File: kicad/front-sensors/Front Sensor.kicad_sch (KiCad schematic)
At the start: 10 parts, among them J8301 ZX-SH1_0-7PWT, U8301 VL53L7CHV0GC/1

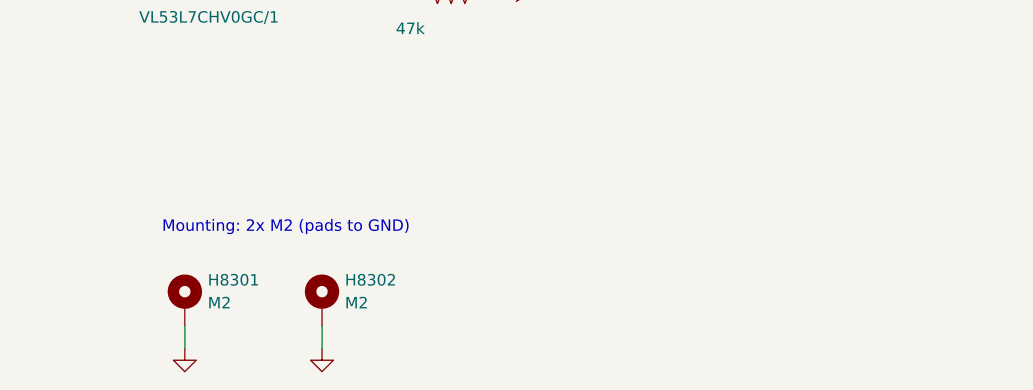
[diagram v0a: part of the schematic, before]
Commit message: LiDAR header, shunt, holes, Hall connector, INT pullup fix
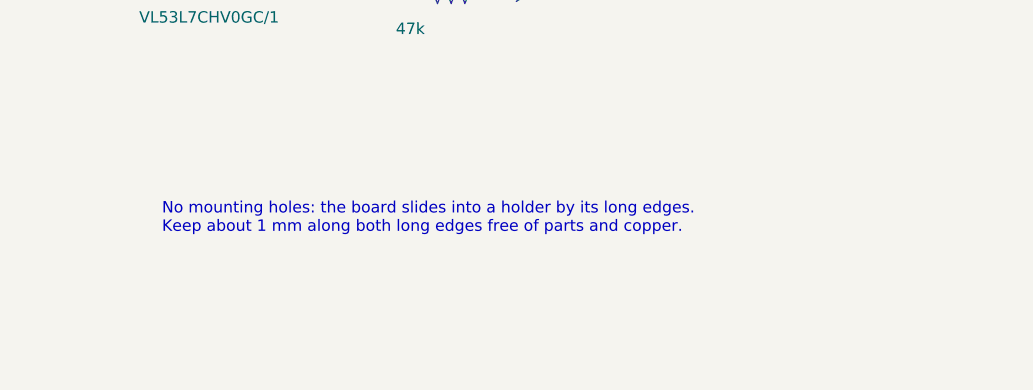
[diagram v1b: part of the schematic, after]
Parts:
- removed H8301, H8302: M2, MountingHole:MountingHole_2.2mm_M2_Pad, symbol Mechanical:MountingHole_Pad
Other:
- note added: "No mounting holes: the board slides into a holder by its long edges. Keep about 1 mm along both long edges free of parts and copper."
- note removed: "Mounting: 2x M2 (pads to GND)"
